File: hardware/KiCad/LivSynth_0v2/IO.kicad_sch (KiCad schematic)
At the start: 95 parts, among them J1 PJ398SM, J10 Jumper, J11 Jumper, J2 PJ398SM, J20 IDC, J3 PJ398SM, J4 IDC, Q3 2N3904, Q4 2N3904, SW5 SW_Push, U10 74HC165, U11 PCA9685PW, U12 PCA9685PW, U13 74HC165, U2 LM386

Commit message: progress 2023-01-21
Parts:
- LS1: value 8R (<32R) 1W -> LSM-50M/NO-B 8R (<32R) 1W; footprint (none) -> SloBlo:LSM-50M NO-B
- NT1, NT3, NT4: footprint NetTie:NetTie-2_SMD_Pad2.0mm -> NetTie:NetTie-2_SMD_Pad0.5mm
- U11, U12: LCSC C2688894 -> C2678753
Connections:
- net LED1_B: now also U12.8 (LED2); no longer U11.21 (LED14)
- net LED1_G: now also U12.7 (LED1); no longer U11.20 (LED13)
- net LED1_R: now also U12.6 (LED0); no longer U11.19 (LED12)
- net P1_B: now also U12.11 (LED5); no longer U12.8 (LED2)
- net P1_G: now also U12.10 (LED4); no longer U12.7 (LED1)
- net P1_R: now also U12.9 (LED3); no longer U12.6 (LED0)
- net P2_B: now also U12.15 (LED8); no longer U12.11 (LED5)
- net P2_G: now also U12.13 (LED7); no longer U12.10 (LED4)
- net P2_R: now also U12.12 (LED6); no longer U12.9 (LED3)
- net P3_B: now also U12.18 (LED11); no longer U12.15 (LED8)
- net P3_G: now also U12.17 (LED10); no longer U12.13 (LED7)
- net P3_R: now also U12.16 (LED9); no longer U12.12 (LED6)
- net P4_B: now also U12.21 (LED14); no longer U12.18 (LED11)
- net P4_G: now also U12.20 (LED13); no longer U12.17 (LED10)
- net P4_R: now also U12.19 (LED12); no longer U12.16 (LED9)
- net P5_B: now also U11.8 (LED2); no longer U12.21 (LED14)
- net P5_G: now also U11.7 (LED1); no longer U12.20 (LED13)
- net P5_R: now also U11.6 (LED0); no longer U12.19 (LED12)
- net P6_B: now also U11.11 (LED5); no longer U11.8 (LED2)
- net P6_G: now also U11.10 (LED4); no longer U11.7 (LED1)
- net P6_R: now also U11.9 (LED3); no longer U11.6 (LED0)
- net P7_B: now also U11.15 (LED8); no longer U11.11 (LED5)
- net P7_G: now also U11.13 (LED7); no longer U11.10 (LED4)
- net P7_R: now also U11.12 (LED6); no longer U11.9 (LED3)
- net P8_B: now also U11.18 (LED11); no longer U11.15 (LED8)
- net P8_G: now also U11.17 (LED10); no longer U11.13 (LED7)
- net P8_R: now also U11.16 (LED9); no longer U11.12 (LED6)
- net P9_B: now also U11.21 (LED14); no longer U11.18 (LED11)
- net P9_G: now also U11.20 (LED13); no longer U11.17 (LED10)
- net P9_R: now also U11.19 (LED12); no longer U11.16 (LED9)
- net at C2.1: now also J1.3; no longer RV6.2
- net at C2.2: now also RV6.2; no longer J1.3
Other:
- moved on the sheet: C2
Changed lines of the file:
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@@
     (effects (font (size 1.27 1.27)) (justify right bottom))
   )
-  (label "P5_G" (at 83.82 66.675 0)
+  (label "P5_G" (at 149.86 36.195 0)
     (effects (font (size 1.27 1.27)) (justify left bottom))
   )
@@
     (effects (font (size 1.27 1.27)) (justify right bottom))
   )
-  (label "LED1_B" (at 149.86 69.215 0)
+  (label "LED1_B" (at 83.82 38.735 0)
     (effects (font (size 1.27 1.27)) (justify left bottom))
   )
@@
     (effects (font (size 1.27 1.27)) (justify left bottom))
   )
-  (label "P2_B" (at 83.82 46.355 0)
+  (label "P2_B" (at 83.82 53.975 0)
     (effects (font (size 1.27 1.27)) (justify left bottom))
   )
@@
     (effects (font (size 1.27 1.27)) (justify right bottom))
   )
-  (label "P6_G" (at 149.86 36.195 0)
+  (label "P6_G" (at 149.86 43.815 0)
     (effects (font (size 1.27 1.27)) (justify left bottom))
   )
@@
     (effects (font (size 1.27 1.27)) (justify right bottom))
   )
-  (label "P5_R" (at 83.82 64.135 0)
-    (effects (font (size 1.27 1.27)) (justify left bottom))
-  )
-  (label "LED1_G" (at 149.86 66.675 0)
+  (label "P5_R" (at 149.86 33.655 0)
+    (effects (font (size 1.27 1.27)) (justify left bottom))
+  )
+  (label "LED1_G" (at 83.82 36.195 0)
     (effects (font (size 1.27 1.27)) (justify left bottom))
   )
@@
     (effects (font (size 1.27 1.27)) (justify right bottom))
   )
-  (label "P7_G" (at 149.86 43.815 0)
-    (effects (font (size 1.27 1.27)) (justify left bottom))
-  )
-  (label "P8_R" (at 149.86 48.895 0)
-    (effects (font (size 1.27 1.27)) (justify left bottom))
-  )
-  (label "P7_R" (at 149.86 41.275 0)
-    (effects (font (size 1.27 1.27)) (justify left bottom))
-  )
-  (label "P3_G" (at 83.82 51.435 0)
+  (label "P7_G" (at 149.86 51.435 0)
+    (effects (font (size 1.27 1.27)) (justify left bottom))
+  )
+  (label "P8_R" (at 149.86 56.515 0)
+    (effects (font (size 1.27 1.27)) (justify left bottom))
+  )
+  (label "P7_R" (at 149.86 48.895 0)
+    (effects (font (size 1.27 1.27)) (justify left bottom))
+  )
+  (label "P3_G" (at 83.82 59.055 0)
     (effects (font (size 1.27 1.27)) (justify left bottom))
   )
@@
     (effects (font (size 1.27 1.27)) (justify right bottom))
   )
-  (label "P1_B" (at 83.82 38.735 0)
+  (label "P1_B" (at 83.82 46.355 0)
     (effects (font (size 1.27 1.27)) (justify left bottom))
   )
@@
     (effects (font (size 1.27 1.27)) (justify right bottom))
   )
-  (label "P4_R" (at 83.82 56.515 0)
+  (label "P4_R" (at 83.82 64.135 0)
     (effects (font (size 1.27 1.27)) (justify left bottom))
   )
@@
     (effects (font (size 1.27 1.27)) (justify right bottom))
   )
-  (label "P5_B" (at 83.82 69.215 0)
+  (label "P5_B" (at 149.86 38.735 0)
     (effects (font (size 1.27 1.27)) (justify left bottom))
   )
@@
     (effects (font (size 1.27 1.27)) (justify left bottom))
   )
-  (label "P6_R" (at 149.86 33.655 0)
+  (label "P6_R" (at 149.86 41.275 0)
     (effects (font (size 1.27 1.27)) (justify left bottom))
   )
@@
     (effects (font (size 1.27 1.27)) (justify right bottom))
   )
-  (label "P2_R" (at 83.82 41.275 0)
-    (effects (font (size 1.27 1.27)) (justify left bottom))
-  )
-  (label "P3_B" (at 83.82 53.975 0)
+  (label "P2_R" (at 83.82 48.895 0)
+    (effects (font (size 1.27 1.27)) (justify left bottom))
+  )
+  (label "P3_B" (at 83.82 61.595 0)
     (effects (font (size 1.27 1.27)) (justify left bottom))
   )
@@
     (effects (font (size 1.27 1.27)) (justify right bottom))
   )
-  (label "P9_R" (at 149.86 56.515 0)
-    (effects (font (size 1.27 1.27)) (justify left bottom))
-  )
-  (label "P3_R" (at 83.82 48.895 0)
-    (effects (font (size 1.27 1.27)) (justify left bottom))
-  )
-  (label "P6_B" (at 149.86 38.735 0)
+  (label "P9_R" (at 149.86 64.135 0)
+    (effects (font (size 1.27 1.27)) (justify left bottom))
+  )
+  (label "P3_R" (at 83.82 56.515 0)
+    (effects (font (size 1.27 1.27)) (justify left bottom))
+  )
+  (label "P6_B" (at 149.86 46.355 0)
     (effects (font (size 1.27 1.27)) (justify left bottom))
   )
@@
     (effects (font (size 1.27 1.27)) (justify right bottom))
   )
-  (label "P2_G" (at 83.82 43.815 0)
+  (label "P2_G" (at 83.82 51.435 0)
     (effects (font (size 1.27 1.27)) (justify left bottom))
   )
@@
     (effects (font (size 1.27 1.27)) (justify left bottom))
   )
-  (label "P8_B" (at 149.86 53.975 0)
+  (label "P8_B" (at 149.86 61.595 0)
     (effects (font (size 1.27 1.27)) (justify left bottom))
   )
@@
     (effects (font (size 1.27 1.27)) (justify right bottom))
   )
-  (label "P1_R" (at 83.82 33.655 0)
-    (effects (font (size 1.27 1.27)) (justify left bottom))
-  )
-  (label "P9_B" (at 149.86 61.595 0)
-    (effects (font (size 1.27 1.27)) (justify left bottom))
-  )
-  (label "P9_G" (at 149.86 59.055 0)
+  (label "P1_R" (at 83.82 41.275 0)
+    (effects (font (size 1.27 1.27)) (justify left bottom))
+  )
+  (label "P9_B" (at 149.86 69.215 0)
+    (effects (font (size 1.27 1.27)) (justify left bottom))
+  )
+  (label "P9_G" (at 149.86 66.675 0)
     (effects (font (size 1.27 1.27)) (justify left bottom))
   )
@@
     (effects (font (size 1.27 1.27)) (justify right bottom))
   )
-  (label "P8_G" (at 149.86 51.435 0)
+  (label "P8_G" (at 149.86 59.055 0)
     (effects (font (size 1.27 1.27)) (justify left bottom))
   )
@@
     (effects (font (size 1.27 1.27)) (justify right bottom))
   )
-  (label "P7_B" (at 149.86 46.355 0)
-    (effects (font (size 1.27 1.27)) (justify left bottom))
-  )
-  (label "P1_G" (at 83.82 36.195 0)
-    (effects (font (size 1.27 1.27)) (justify left bottom))
-  )
-  (label "LED1_R" (at 149.86 64.135 0)
+  (label "P7_B" (at 149.86 53.975 0)
+    (effects (font (size 1.27 1.27)) (justify left bottom))
+  )
+  (label "P1_G" (at 83.82 43.815 0)
+    (effects (font (size 1.27 1.27)) (justify left bottom))
+  )
+  (label "LED1_R" (at 83.82 33.655 0)
     (effects (font (size 1.27 1.27)) (justify left bottom))
   )
@@
     (effects (font (size 1.27 1.27)) (justify left bottom))
   )
-  (label "P4_G" (at 83.82 59.055 0)
+  (label "P4_G" (at 83.82 66.675 0)
     (effects (font (size 1.27 1.27)) (justify left bottom))
   )
@@
     (effects (font (size 1.27 1.27)) (justify right bottom))
   )
-  (label "P4_B" (at 83.82 61.595 0)
+  (label "P4_B" (at 83.82 69.215 0)
     (effects (font (size 1.27 1.27)) (justify left bottom))
   )
@@
       (effects (font (size 1.27 1.27)) hide)
     )
-    (property "LCSC" "C2688894" (id 4) (at 62.23 51.435 0)
+    (property "LCSC" "C2678753" (id 4) (at 62.23 51.435 0)
       (effects (font (size 1.27 1.27)) hide)
     )
@@
     (pin "1")
   )
-  (symbol (lib_id "Device:C_Polarized_Small") (at 344.17 31.115 90) (unit 1)
-    (in_bom yes) (on_board yes) (fields_autoplaced)
-    (property "Reference" "C2" (id 0) (at 343.6239 24.13 90))
-    (property "Value" "1u" (id 1) (at 343.6239 26.67 90))
+  (symbol (lib_id "Device:C_Polarized_Small") (at 344.17 31.115 270) (mirror x) (unit 1)
+    (in_bom yes) (on_board yes) (fields_autoplaced)
+    (property "Reference" "C2" (id 0) (at 344.7161 24.13 90))
+    (property "Value" "1u" (id 1) (at 344.7161 26.67 90))
     (property "Footprint" "Capacitor_THT:C_Rect_L7.2mm_W5.5mm_P5.00mm_FKS2_FKP2_MKS2_MKP2" (id 2) (at 344.17 31.115 0)
       (effects (font (size 1.27 1.27)) hide)
@@
       (effects (font (size 1.27 1.27)) (justify right) hide)
     )
-    (property "Footprint" "NetTie:NetTie-2_SMD_Pad2.0mm" (id 2) (at 186.69 191.77 0)
+    (property "Footprint" "NetTie:NetTie-2_SMD_Pad0.5mm" (id 2) (at 186.69 191.77 0)
       (effects (font (size 1.27 1.27)) hide)
     )
@@
   )
   (symbol (lib_id "Device:Speaker") (at 387.35 66.675 0) (unit 1)
-    (in_bom yes) (on_board yes) (fields_autoplaced)
-    (property "Reference" "LS1" (id 0) (at 391.795 66.6749 0)
-      (effects (font (size 1.27 1.27)) (justify left))
-    )
-    (property "Value" "8R (<32R) 1W" (id 1) (at 391.795 69.2149 0)
-      (effects (font (size 1.27 1.27)) (justify left))
-    )
-    (property "Footprint" "" (id 2) (at 387.35 71.755 0)
+    (in_bom yes) (on_board yes)
+    (property "Reference" "LS1" (id 0) (at 391.795 67.945 0)
+      (effects (font (size 1.27 1.27)) (justify left))
+    )
+    (property "Value" "LSM-50M/NO-B 8R (<32R) 1W" (id 1) (at 374.015 74.295 0)
+      (effects (font (size 1.27 1.27)) (justify left))
+    )
+    (property "Footprint" "SloBlo:LSM-50M NO-B" (id 2) (at 387.35 71.755 0)
       (effects (font (size 1.27 1.27)) hide)
     )
@@
   )
   (symbol (lib_id "Connector:Conn_01x02_Female") (at 373.38 66.675 0) (mirror y) (unit 1)
-    (in_bom yes) (on_board yes)
+    (in_bom yes) (on_board no)
     (property "Reference" "J20" (id 0) (at 375.92 60.325 0))
     (property "Value" "IDC" (id 1) (at 375.92 62.865 0))
@@
       (effects (font (size 1.27 1.27)) (justify right))
     )
-    (property "Footprint" "NetTie:NetTie-2_SMD_Pad2.0mm" (id 2) (at 376.555 38.735 0)
+    (property "Footprint" "NetTie:NetTie-2_SMD_Pad0.5mm" (id 2) (at 376.555 38.735 0)
       (effects (font (size 1.27 1.27)) hide)
     )
@@
       (effects (font (size 1.27 1.27)) (justify left) hide)
     )
-    (property "Footprint" "NetTie:NetTie-2_SMD_Pad2.0mm" (id 2) (at 124.46 191.77 0)
+    (property "Footprint" "NetTie:NetTie-2_SMD_Pad0.5mm" (id 2) (at 124.46 191.77 0)
       (effects (font (size 1.27 1.27)) hide)
     )
@@
       (effects (font (size 1.27 1.27)) hide)
     )
-    (property "LCSC" "C2688894" (id 4) (at 128.27 51.435 0)
-      (effects (font (size 1.27 1.27)) hide)
-    )
+    (property "LCSC" "C2678753" (id 4) (at 128.27 51.435 0)
+      (effects (font (size 1.27 1.27)) hide)
+    )

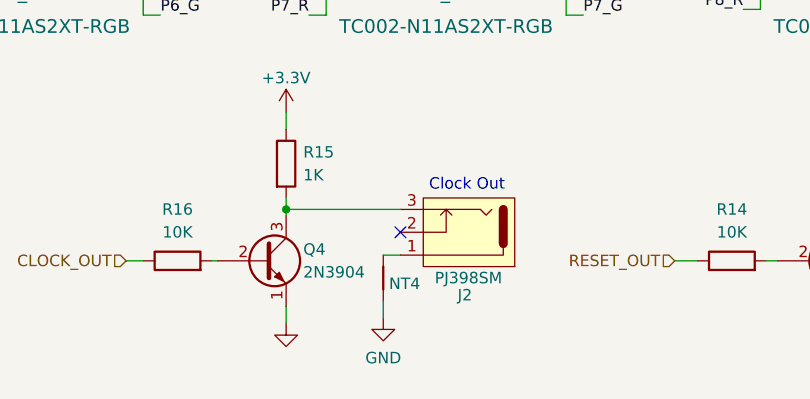
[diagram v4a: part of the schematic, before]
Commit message: LCSC component looked up
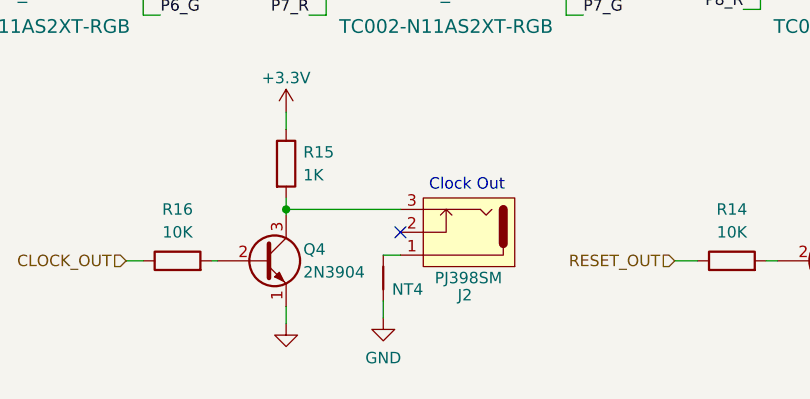
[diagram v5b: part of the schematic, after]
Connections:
- net GND: now also NT4.1; no longer NT4.2
- net at J2.1: now also NT4.2; no longer NT4.1
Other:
- moved on the sheet: NT4
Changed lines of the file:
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@@
     (pin "1")
   )
-  (symbol (lib_id "Device:NetTie_2") (at 124.46 191.77 270) (unit 1)
+  (symbol (lib_id "Device:NetTie_2") (at 124.46 191.77 90) (unit 1)
     (in_bom yes) (on_board yes)
-    (property "Reference" "NT4" (id 0) (at 125.095 192.405 90)
+    (property "Reference" "NT4" (id 0) (at 128.905 193.04 90)
       (effects (font (size 1.27 1.27)) (justify left))
     )
-    (property "Value" "NetTie_2" (id 1) (at 125.095 194.945 90)
+    (property "Value" "NetTie_2" (id 1) (at 123.825 188.595 90)
       (effects (font (size 1.27 1.27)) (justify left) hide)
     )

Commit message: Geographical reannotate
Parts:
- renumbered C7 to C14, C8 to C15, C9 to C17, C6 to C23, C21 to C24, C19 to C28, C22 to C29, C52 to C43, C53 to C58, C54 to C59, C5 to C6, C38 to C61, C42 to C62, C2 to C9, D5 to D3, J2 to J1, J10 to J13, J11 to J14, J3 to J2, J1 to J3, NT1 to NT2, Q3 to Q6, Q4 to Q7, R106 to R100, R95 to R101, R99 to R102, R107 to R103, R110 to R104, R100 to R105, R103 to R107, R104 to R108, R105 to R109, R108 to R110, R109 to R111, R94 to R112, R98 to R113, R97 to R114, R114 to R116, R113 to R117, R117 to R118, R115 to R119, R116 to R120, R118 to R121, R125 to R122, R126 to R123, R128 to R124, R127 to R125, R119 to R126, R121 to R127, R120 to R128, R122 to R129, R123 to R130, R124 to R131, R10 to R14, R8 to R15, R9 to R16, R15 to R25, R13 to R27, R14 to R29, R16 to R30, R33 to R40, R34 to R41, R59 to R61, R79 to R88, R82 to R89, R81 to R90, R80 to R91, R111 to R92, R112 to R93, R96 to R97, R101 to R98, R102 to R99, RGB_Pot8 to RGB_Pot7, RGB_Pot7 to RGB_Pot8, RV22 to RV21, RV6 to RV3, RV1 to RV4, SW5 to SW6, U11 to U10, U12 to U11, U10 to U13, U13 to U14, U2 to U3

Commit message: Order placement 2023-01-29
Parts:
- J20: now left out of the parts list
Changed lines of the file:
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@@
   )
   (symbol (lib_id "Connector:Conn_01x02_Female") (at 373.38 66.675 0) (mirror y) (unit 1)
-    (in_bom yes) (on_board no)
+    (in_bom no) (on_board no)
     (property "Reference" "J20" (id 0) (at 375.92 60.325 0))
     (property "Value" "IDC" (id 1) (at 375.92 62.865 0))

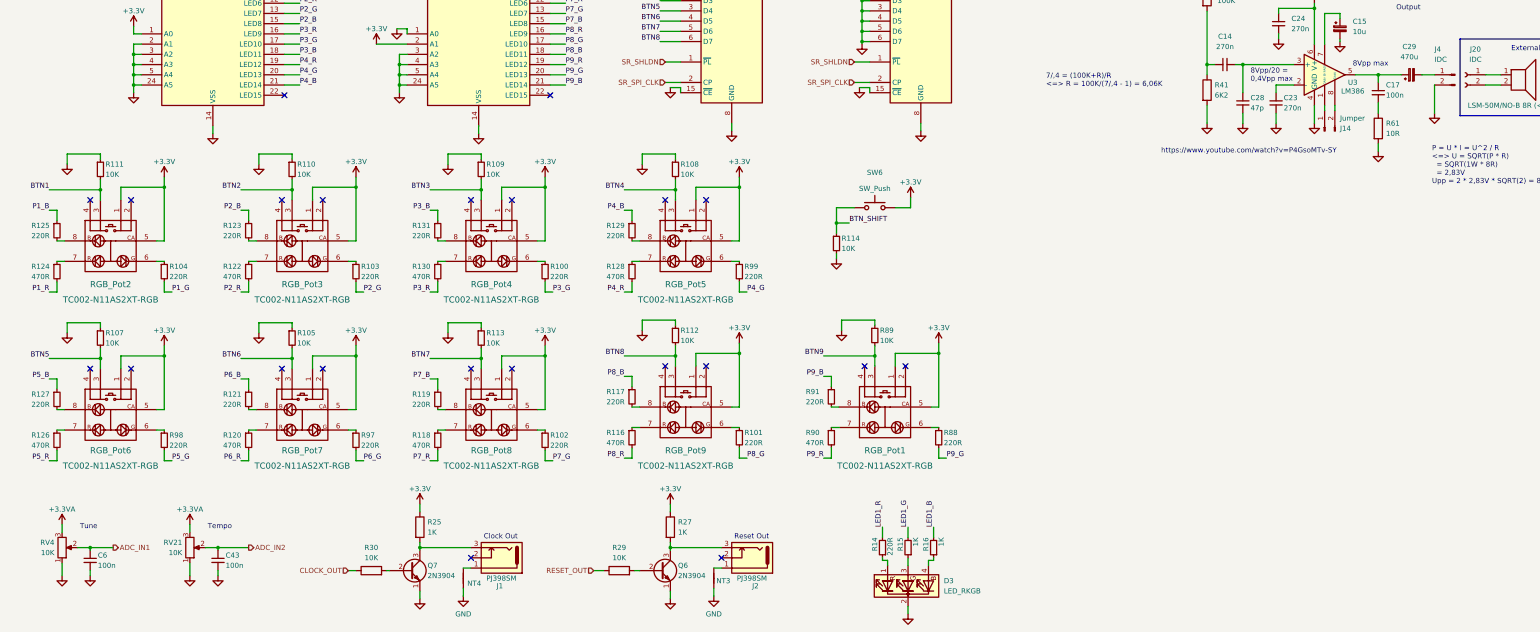
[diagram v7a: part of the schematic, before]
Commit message: Reduce EG cap to 4u7 Reduce LFO cap to 220n VCO R23: 470K, C13: 10n
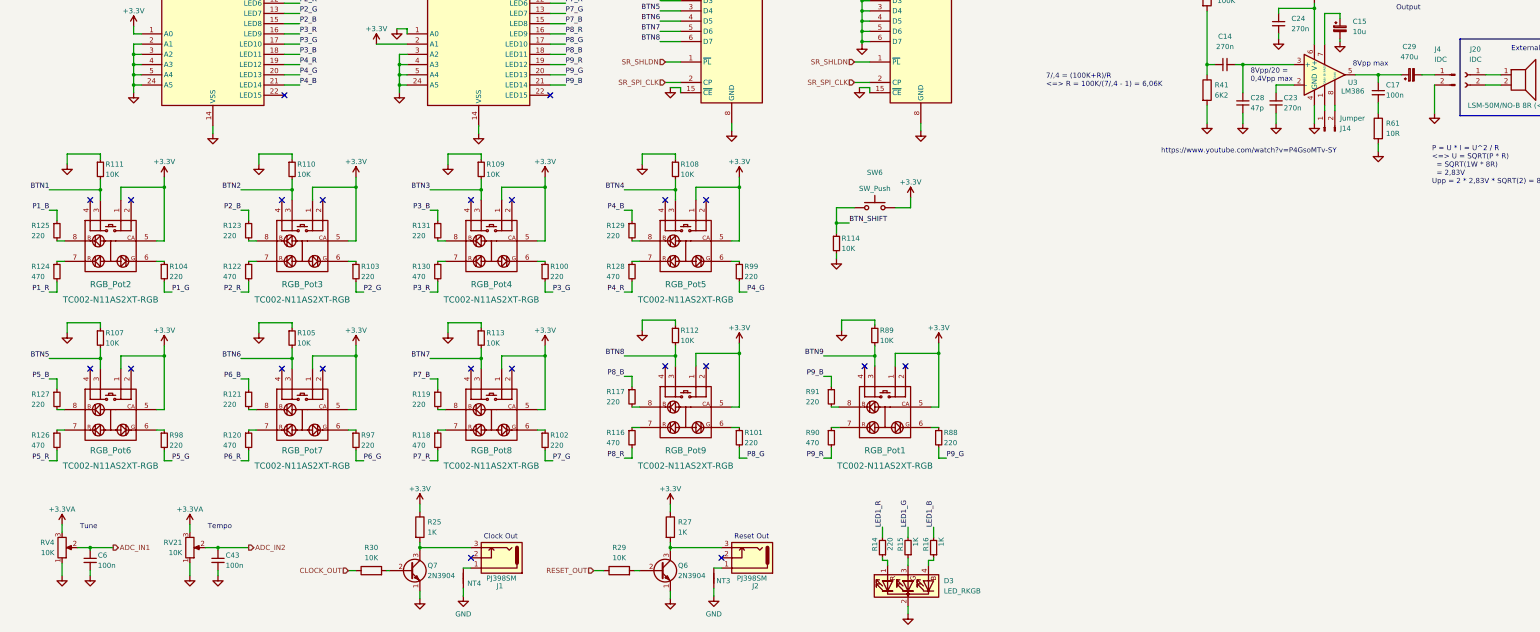
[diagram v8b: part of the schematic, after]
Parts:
- R100, R101, R102, R103, R104, R117, R119, R121, R123, R125, R127, R129, R131, R14, R88, R91, R97, R98, R99: value 220R -> 220
- R116, R118, R120, R122, R124, R126, R128, R130, R90: value 470R -> 470
